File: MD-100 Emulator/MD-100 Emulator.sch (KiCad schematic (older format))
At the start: 42 parts, among them J1 CPB_Connector, J2 I2CConn, J3 ICSP, Q1 NPN, U1 24LC1025, U2 24LC1025, U3 24LC1025, U4 24LC1025, U5 74HC00, U6 74HC02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

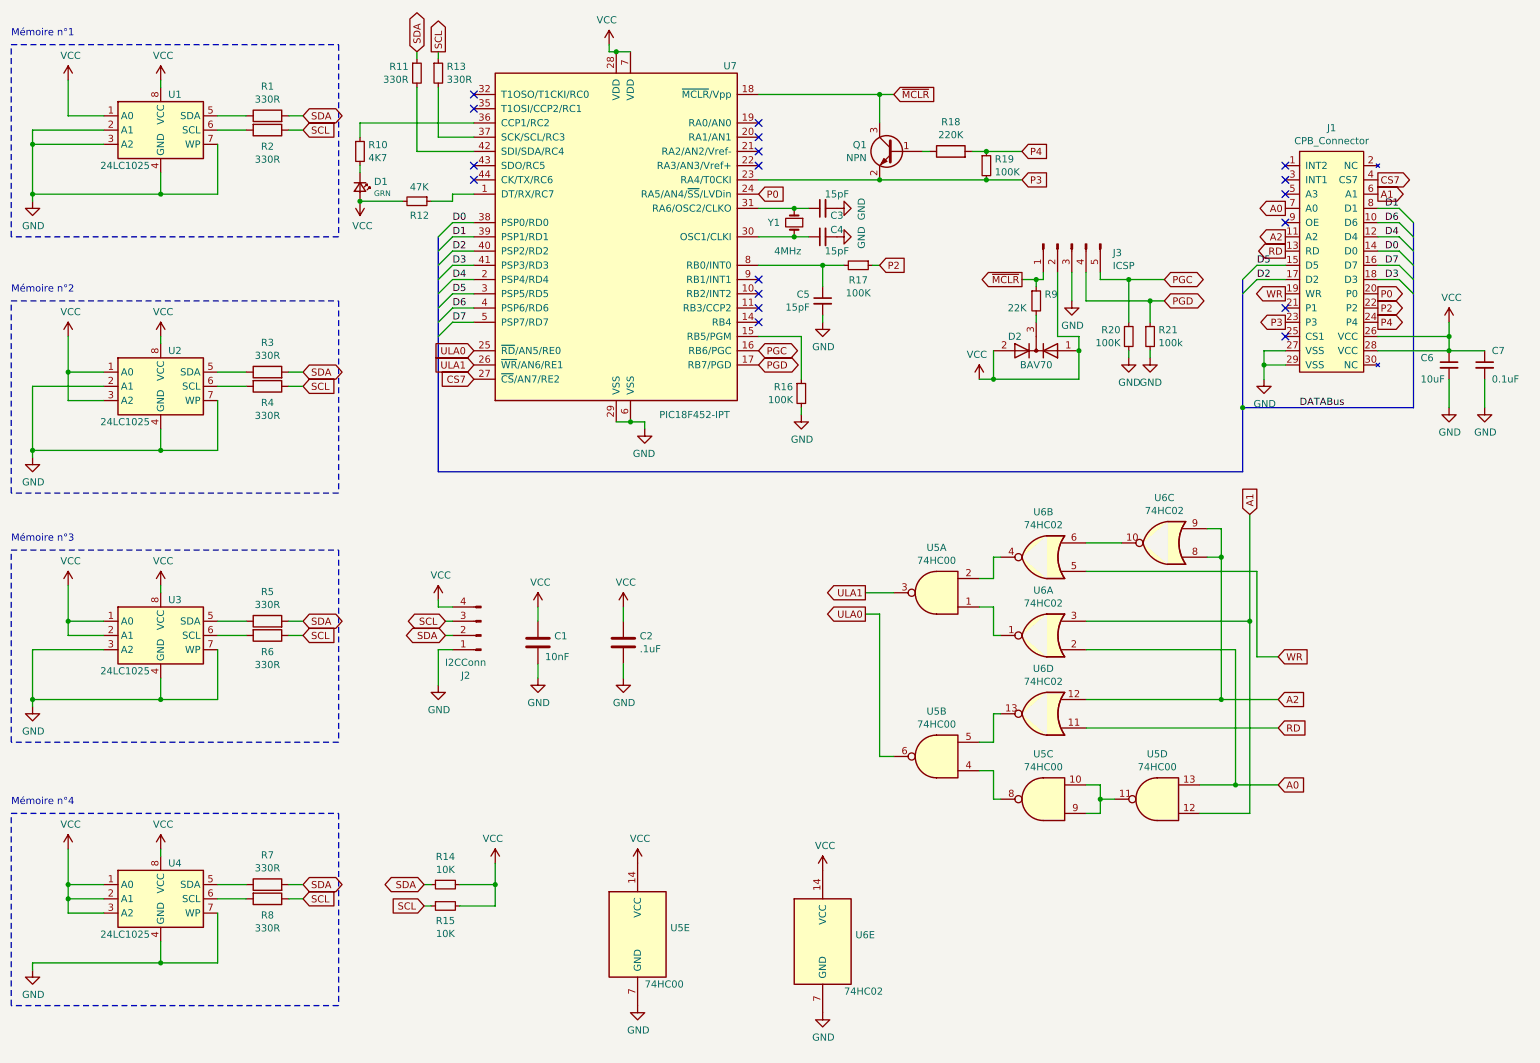
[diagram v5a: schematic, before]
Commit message: Correction en cours du md1000
(pas le proj optimité fait en offline
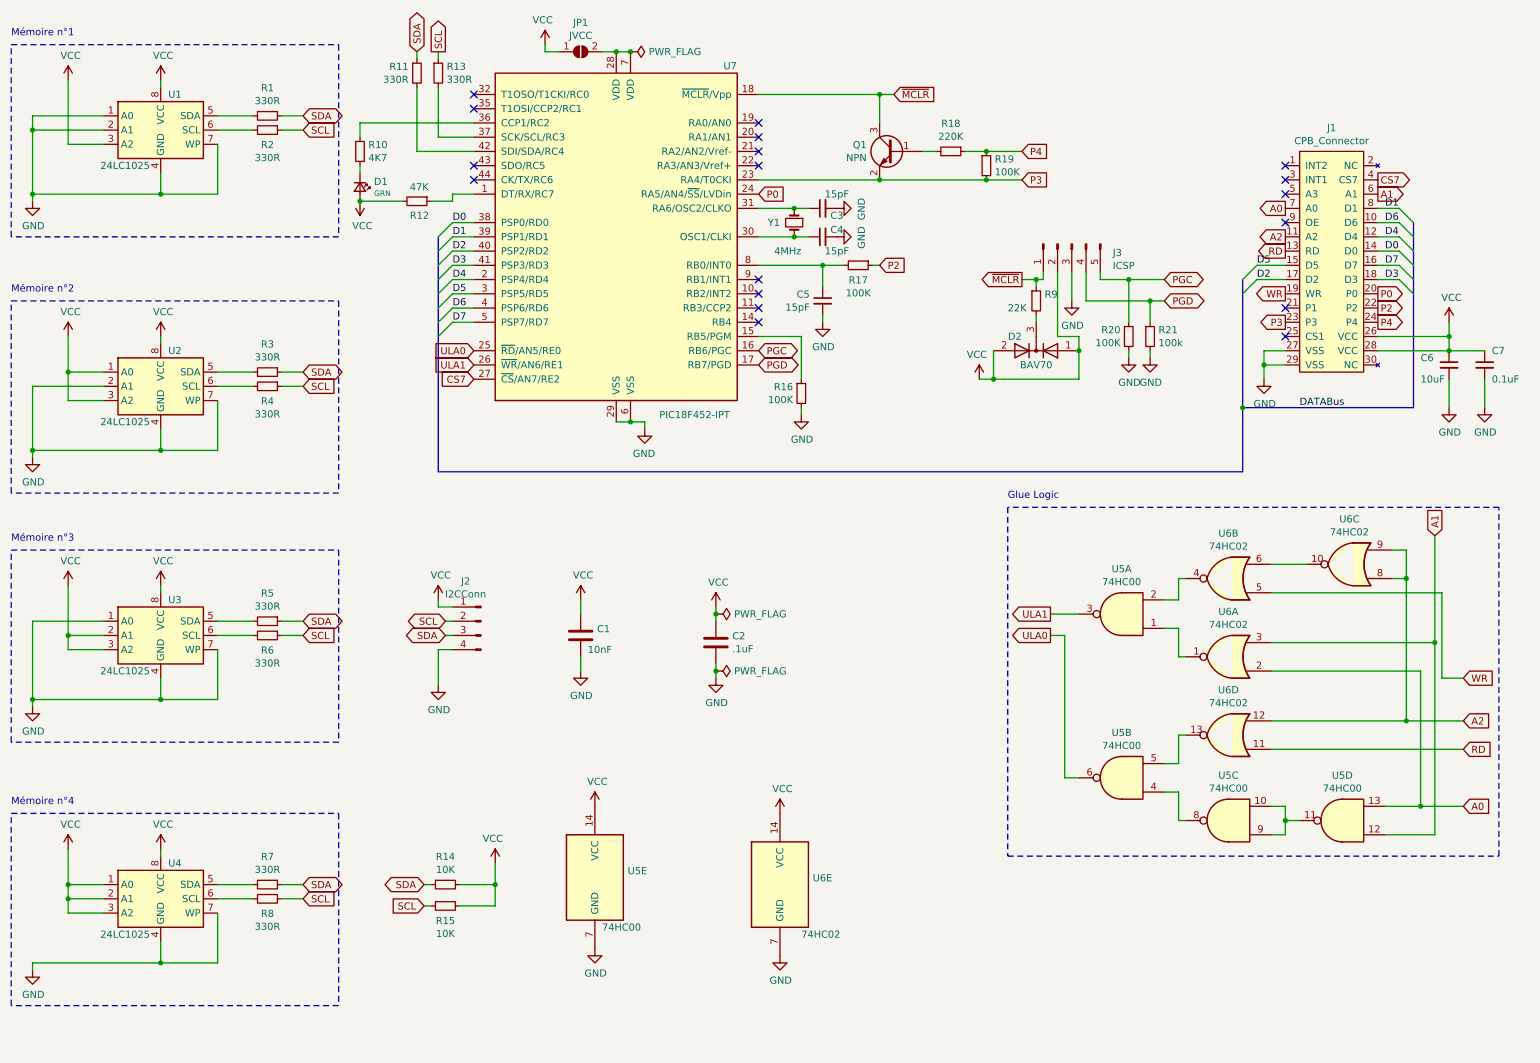
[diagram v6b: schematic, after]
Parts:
- removed R1, R2, R3, R4, R5, R6, R7, R8: 330R, symbol Device:R
- removed R18: 220K, symbol Device:R
- added JP1: JVCC, symbol Jumper:SolderJumper_2_Open
- added R1, R2, R3, R4, R5, R6, R7, R8: 330R, symbol Device:R_Small
- added R18: 220K, symbol Device:R_Small
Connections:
- net GND: now also J2.4 (Pin_4), U1.1 (A0), U3.1 (A0); no longer J2.1 (Pin_1), U1.3 (A2), U3.3 (A2)
- net P4: now also R18.1
- net SCL: now also J2.2 (Pin_2), R2.1, R4.1, R6.1, R8.1; no longer J2.3 (Pin_3)
- net SDA: now also J2.3 (Pin_3), R1.1, R3.1, R5.1, R7.1; no longer J2.2 (Pin_2)
- net VCC: now also J2.1 (Pin_1), U1.3 (A2), U3.3 (A2), JP1.1 (A); no longer J2.4 (Pin_4), U1.1 (A0), U3.1 (A0), U7.28 (VDD), U7.7 (VDD)
- net at U1.5 (SDA): now also R1.2
- net at U1.6 (SCL): now also R2.2
- net at U2.5 (SDA): now also R3.2
- net at U2.6 (SCL): now also R4.2
- net at U3.5 (SDA): now also R5.2
- net at U3.6 (SCL): now also R6.2
- net at U4.5 (SDA): now also R7.2
- net at U4.6 (SCL): now also R8.2
- net at Q1.1 (B): now also R18.2
- new net: JP1.2 (B), U7.28 (VDD), U7.7 (VDD)
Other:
- note added: "Glue Logic"
- moved on the sheet: C1, C2, U5A, U5B, U5C, U5D, U5E, U6A, U6B, U6C, U6D, U6E

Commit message: Amélioré MD100 Emulator
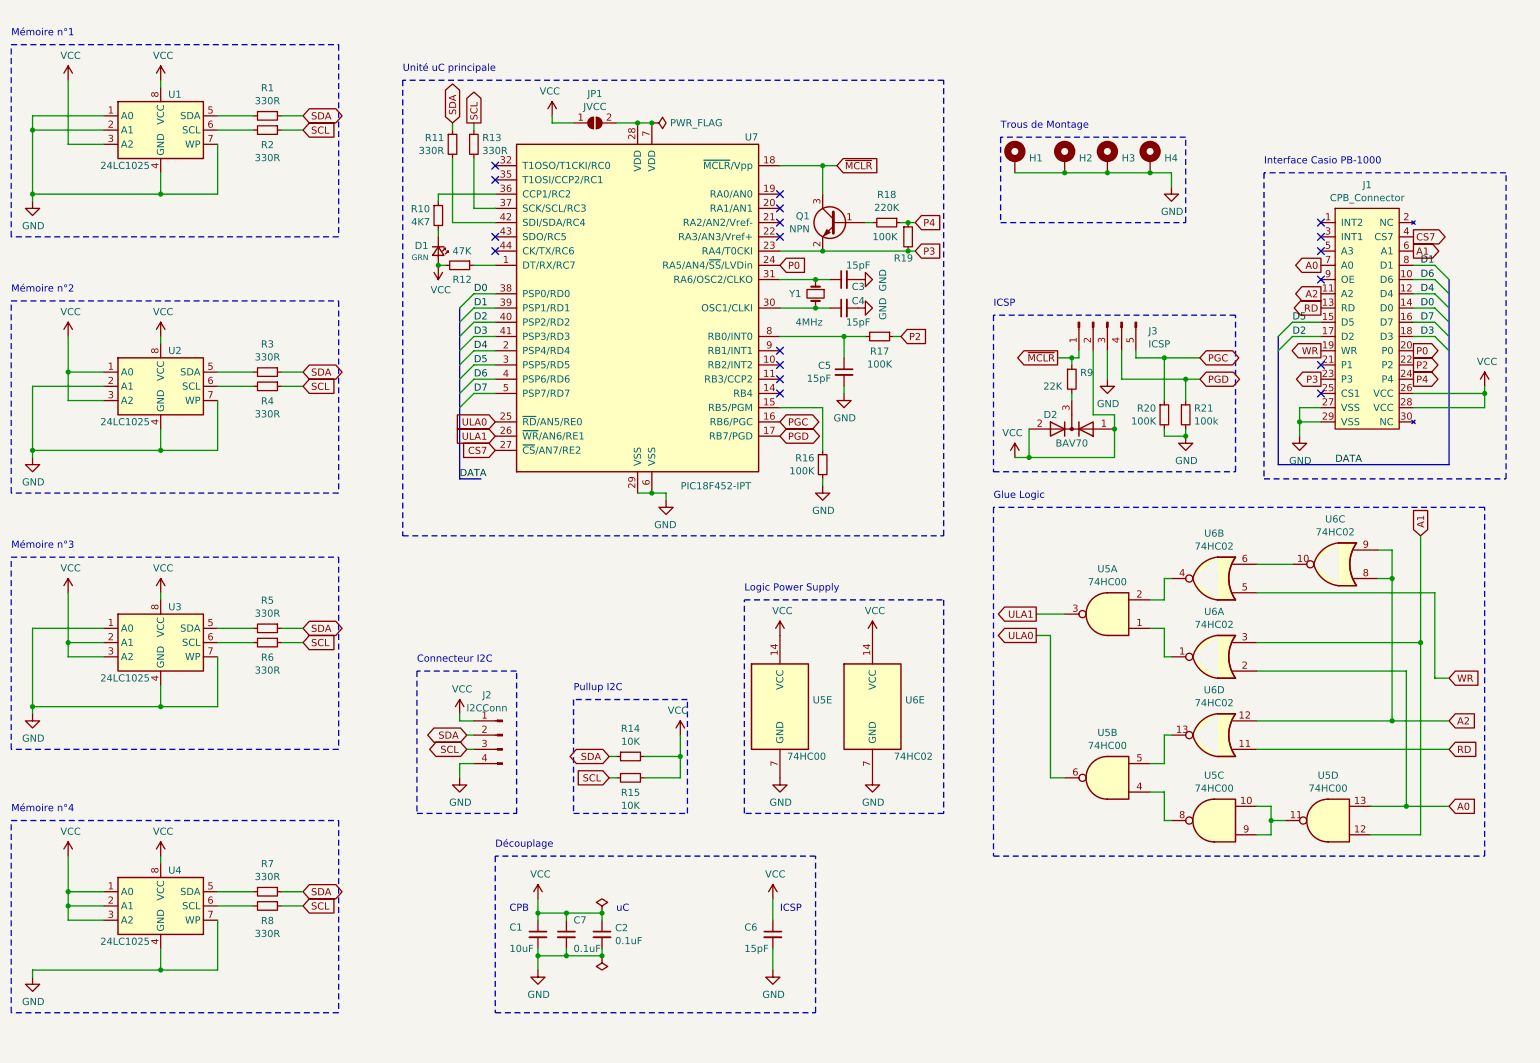
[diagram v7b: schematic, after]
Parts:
- removed C1: 10nF, symbol Device:C
- removed C2: .1uF, symbol Device:C
- added C1: 10uF, Capacitor_SMD:C_0805_2012Metric_Pad1.15x1.40mm_HandSolder, symbol Device:C_Small
- added C2: 0.1uF, Capacitor_SMD:C_0805_2012Metric_Pad1.15x1.40mm_HandSolder, symbol Device:C_Small
- added H1, H2, H3, H4: MountingHole_Pad, MountingHole:MountingHole_3.2mm_M3_Pad_Via, symbol Mechanical:MountingHole_Pad
- C3, C4, C5, C7: footprint (none) -> Capacitor_SMD:C_0805_2012Metric_Pad1.15x1.40mm_HandSolder
- C6: value 10uF -> 15pF; footprint (none) -> Capacitor_SMD:C_0805_2012Metric_Pad1.15x1.40mm_HandSolder
- D1: footprint (none) -> LED_SMD:LED_0805_2012Metric_Pad1.15x1.40mm_HandSolder
- J1: footprint (none) -> hwreverse:Connector_Casio_2x15_1.27_SYSBUS
- J2: footprint (none) -> Connector_PinHeader_2.54mm:PinHeader_1x04_P2.54mm_Horizontal
- J3: footprint (none) -> Connector_PinHeader_2.54mm:PinHeader_1x05_P2.54mm_Horizontal
- JP1: footprint (none) -> Jumper:SolderJumper-2_P1.3mm_Open_RoundedPad1.0x1.5mm
- Q1: footprint (none) -> Package_TO_SOT_SMD:SOT-23
- R1, R10, R11, R12, R13, R14, R15, R16, R17, R18, R19, R2, R20, R21, R3, R4, R5, R6, R7, R8, R9: footprint (none) -> Resistor_SMD:R_0805_2012Metric_Pad1.15x1.40mm_HandSolder
- U1, U2, U3, U4: footprint (none) -> Package_SO:SOIC-8-1EP_3.9x4.9mm_P1.27mm_EP2.29x3mm
- U5, U6: footprint (none) -> Package_SO:SOIC-14_3.9x8.7mm_P1.27mm
- Y1: footprint (none) -> Crystal:Crystal_SMD_HC49-SD_HandSoldering
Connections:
- net GND: now also C1.2, C2.2, H1.1, H2.1, H3.1, H4.1
- net SCL: now also J2.3 (Pin_3); no longer J2.2 (Pin_2)
- net SDA: now also J2.2 (Pin_2); no longer J2.3 (Pin_3)
- net VCC: now also C1.1, C2.1
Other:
- note added: "CPB"
- note added: "Connecteur I2C"
- note added: "Découplage"
- note added: "ICSP"
- note added: "Interface Casio PB-1000"
- note added: "Logic Power Supply"
- note added: "Pullup I2C"
- note added: "Trous de Montage"
- note added: "Unité uC principale"
- note added: "uC"
- moved on the sheet: C3, C4, C5, C6, C7, D1, D2, J1, J2, J3, Q1, R10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

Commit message: Autoroutage de MD100 Version 1
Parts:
- added C8: 0.1uF, Capacitor_SMD:C_0805_2012Metric_Pad1.15x1.40mm_HandSolder, symbol Device:C_Small
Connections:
- net GND: now also C8.2
- net VCC: now also C8.1
- net VDD: now reaches JP1.2 (B), U7.28 (VDD), U7.7 (VDD)
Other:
- note added: "Epaisseur du PCB doit être 0.8mm"
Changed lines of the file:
@@
 Text Notes 4100 6800 0    50   ~ 0
 CPB
-Text Notes 4850 6800 0    50   ~ 0
+Text Notes 4900 6750 0    50   ~ 0
 uC
 Wire Wire Line
@@
 Wire Wire Line
 	750  4800 1250 4800
+$Comp
+L Device:C_Small C8
+U 1 1 5ECA4337
+P 5150 6950
+F 0 "C8" H 5242 6996 50  0000 L CNN
+F 1 "0.1uF" H 5242 6905 50  0000 L CNN
+F 2 "Capacitor_SMD:C_0805_2012Metric_Pad1.15x1.40mm_HandSolder" H 5150 6950 50  0001 C CNN
+F 3 "~" H 5150 6950 50  0001 C CNN
+	1    5150 6950
+	1    0    0    -1
+$EndComp
+Wire Wire Line
+	4750 6800 5150 6800
+Wire Wire Line
+	5150 6800 5150 6850
+Wire Wire Line
+	5150 7050 5150 7100
+Wire Wire Line
+	5150 7100 4750 7100
 Wire Bus Line
 	9500 2750 9500 3650
@@
 Wire Bus Line
 	3750 2550 3750 3750
+Text Notes 9400 1350 0    50   ~ 0
+Epaisseur du PCB doit être 0.8mm
+Text Label 4900 1250 0    50   ~ 0
+VDD
 $EndSCHEMATC
